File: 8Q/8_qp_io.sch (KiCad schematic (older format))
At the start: 0 parts

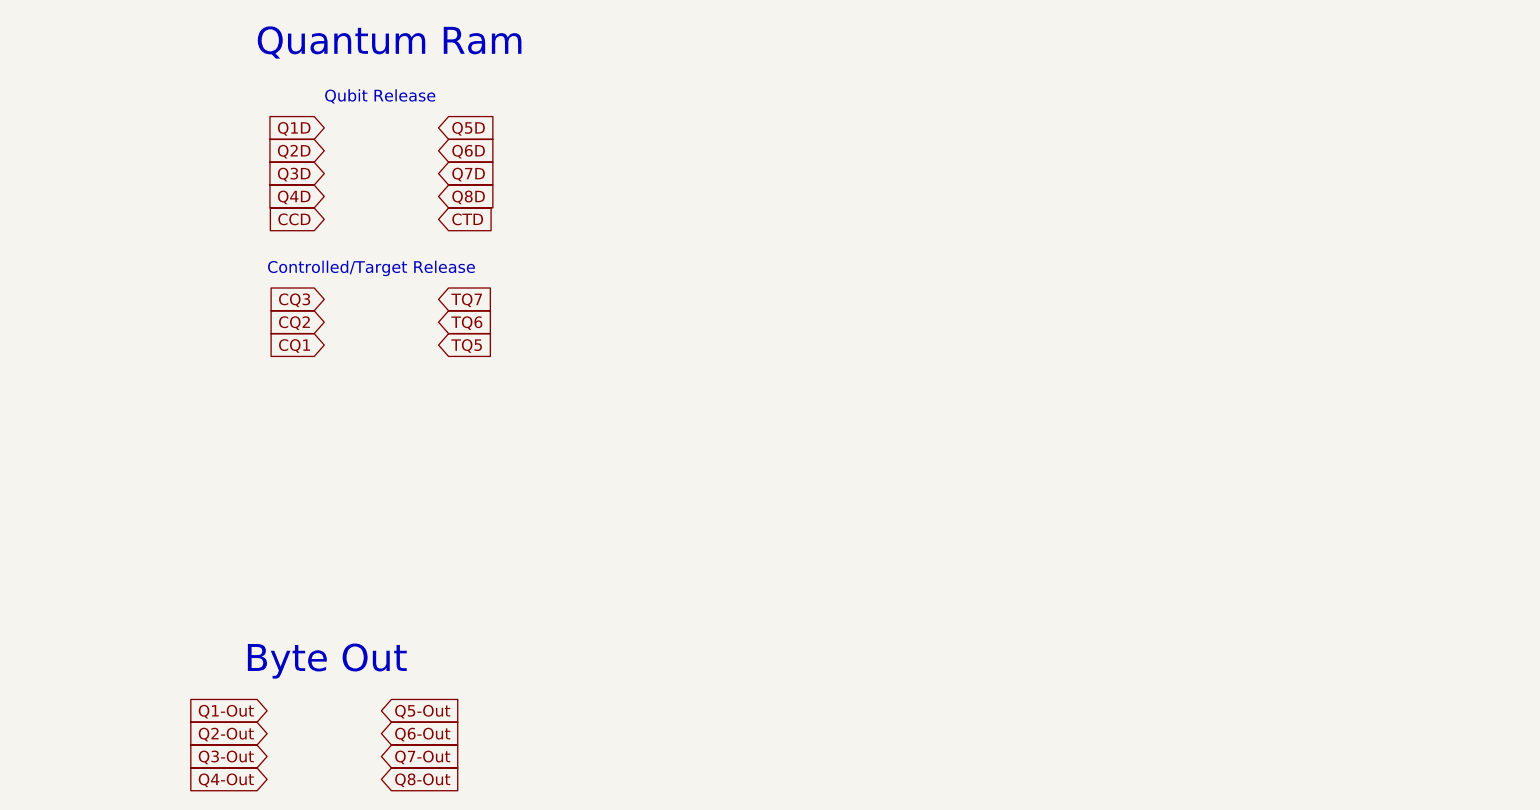
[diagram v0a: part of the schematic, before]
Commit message: modified:   8Q/8Q-cache.lib 	modified:   8Q/8Q.sch 	modified:   8Q/8_qp_io.sch 	new file:   8Q/RAM.sch 	deleted:    8Q/_saved_RAM.sch 	modified:   8Q/cpu.sch 	modified:   8Q/cpu_power.sch 	modified:   8Q/power.sch 	modified:   8Q/preprocessor.sch 	modified:   8Q/qpower.sch 	modified:   8Q/qpu.sch 	new file:   8q.dia 	modified:   README.md 	new file:   docs/source/imgs/8q.png
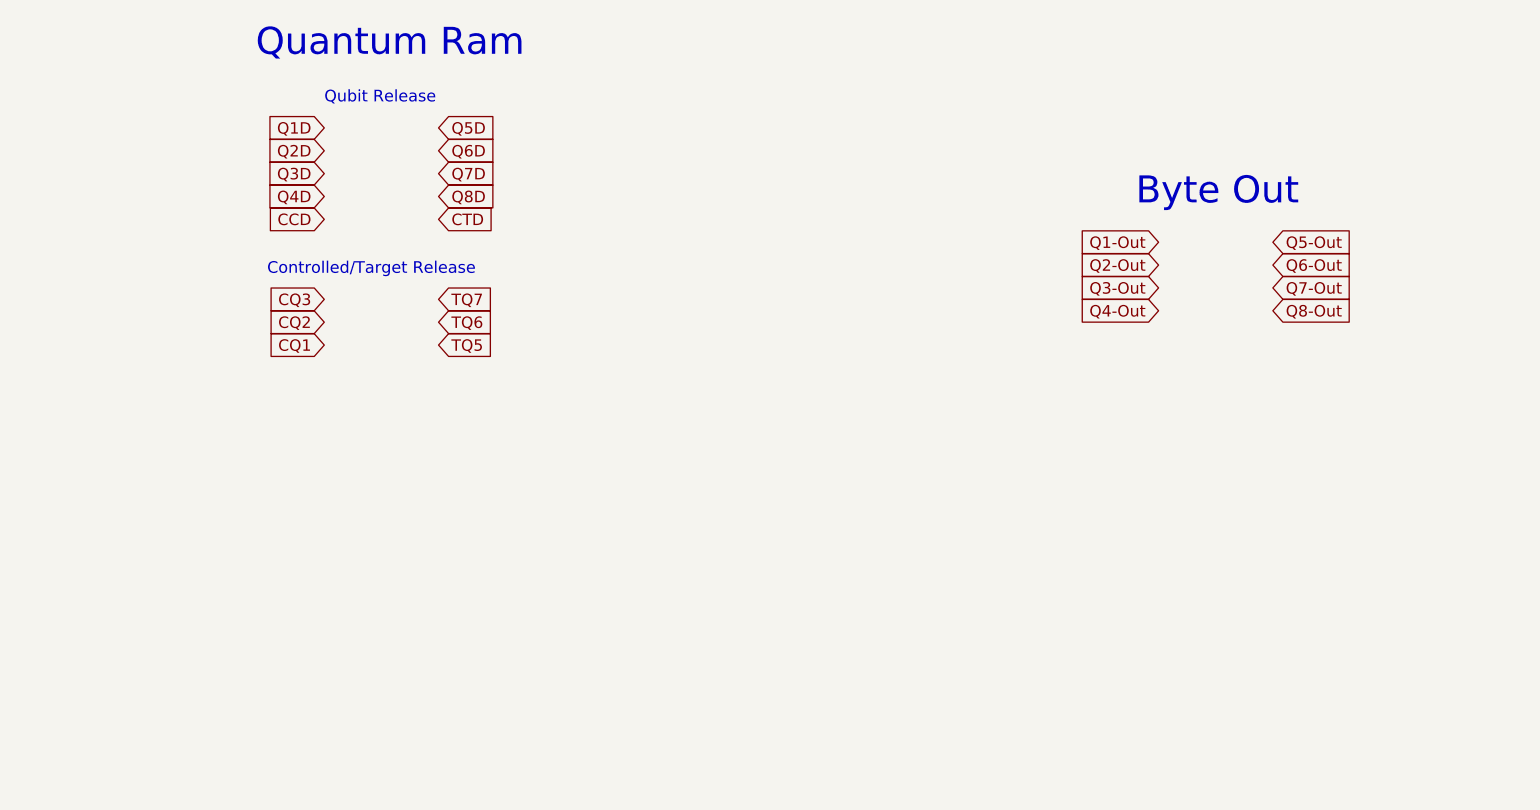
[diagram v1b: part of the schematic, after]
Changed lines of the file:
@@
 $Descr A4 11693 8268
 encoding utf-8
-Sheet 7 8
+Sheet 8 9
 Title ""
 Date ""
@@
 Text GLabel 9700 2450 0    50   Input ~ 0
 SWAP
-Text GLabel 5250 6200 0    50   Input ~ 0
+Text GLabel 9150 4150 0    50   Input ~ 0
 Q1-Out
 Text GLabel 1600 4600 0    50   Input ~ 0
 Q1-S
-Text GLabel 5250 6300 0    50   Input ~ 0
+Text GLabel 9150 4250 0    50   Input ~ 0
 Q2-Out
 Text GLabel 1600 4700 0    50   Input ~ 0
 Q2-S
-Text GLabel 5250 6400 0    50   Input ~ 0
+Text GLabel 9150 4350 0    50   Input ~ 0
 Q3-Out
 Text GLabel 1600 4800 0    50   Input ~ 0
 Q3-S
-Text GLabel 5250 6500 0    50   Input ~ 0
+Text GLabel 9150 4450 0    50   Input ~ 0
 Q4-Out
 Text GLabel 1600 4900 0    50   Input ~ 0
 Q4-S
-Text GLabel 5750 6200 2    50   Input ~ 0
+Text GLabel 9650 4150 2    50   Input ~ 0
 Q5-Out
 Text GLabel 2100 4600 2    50   Input ~ 0
 Q5-S
-Text GLabel 5750 6300 2    50   Input ~ 0
+Text GLabel 9650 4250 2    50   Input ~ 0
 Q6-Out
 Text GLabel 2100 4700 2    50   Input ~ 0
 Q6-S
-Text GLabel 5750 6400 2    50   Input ~ 0
+Text GLabel 9650 4350 2    50   Input ~ 0
 Q7-Out
 Text GLabel 2100 4800 2    50   Input ~ 0
 Q7-S
-Text GLabel 5750 6500 2    50   Input ~ 0
+Text GLabel 9650 4450 2    50   Input ~ 0
 Q8-Out
 Text GLabel 2100 4900 2    50   Input ~ 0
@@
 Text Notes 900  4450 0    118  ~ 0
 Post-Processing Data
-Text Notes 5150 6050 0    118  ~ 0
+Text Notes 9050 4000 0    118  ~ 0
 Byte Out
 Text Notes 1250 1700 0    118  ~ 0

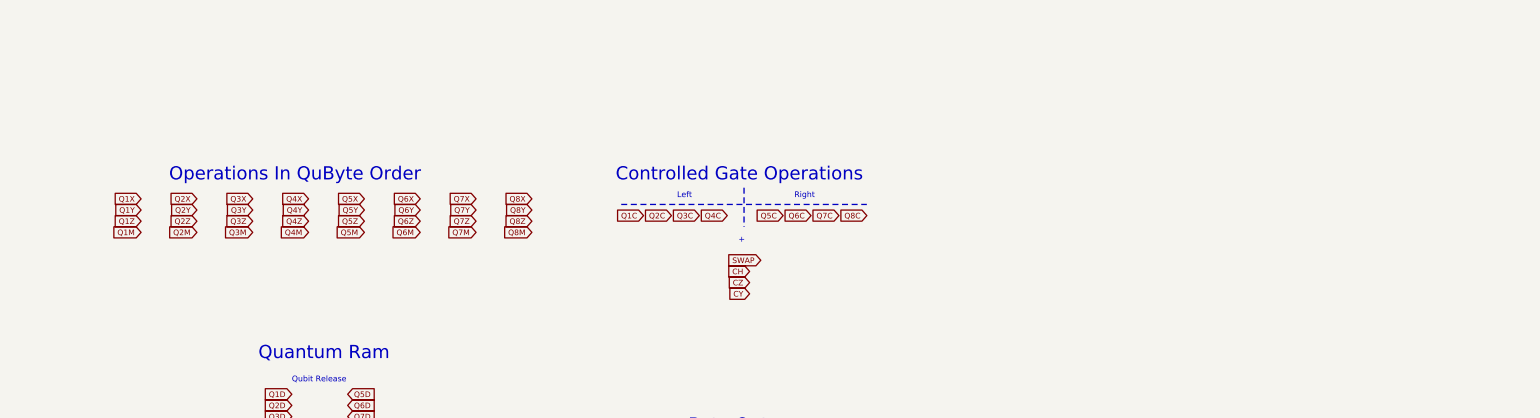
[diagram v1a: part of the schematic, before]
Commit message: modified:   8Q/8Q-cache.lib 	modified:   8Q/8Q.sch 	modified:   8Q/8_qp_io.sch 	modified:   8Q/RAM.sch 	new file:   8Q/control_logic.sch 	modified:   8Q/cpu.sch 	modified:   8Q/cpu_power.sch 	new file:   8Q/inorder.sch 	new file:   8Q/instruction_bus.sch 	new file:   8Q/output_cache.sch 	modified:   8Q/power.sch 	modified:   8Q/preprocessor.sch 	modified:   8Q/qpower.sch 	modified:   8Q/qpu.sch 	new file:   Controller.md 	modified:   QCore.md 	new file:   QPU_Operation.md 	new file:   docs/source/imgs/Screenshot from 2020-07-07 18-04-51.png 	new file:   tools/photon_birth_death.py 	new file:   tools/processor.py
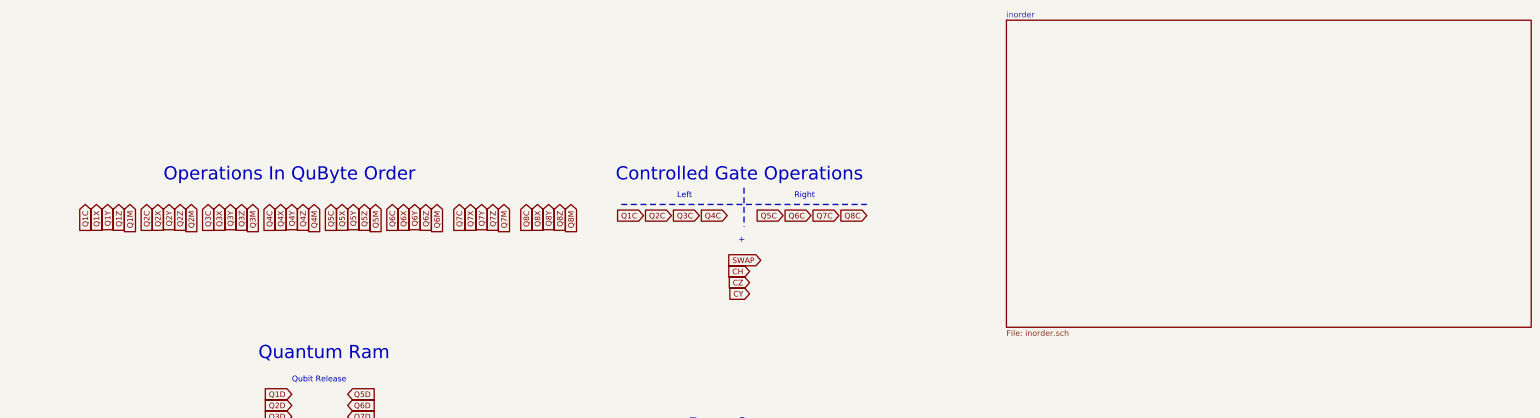
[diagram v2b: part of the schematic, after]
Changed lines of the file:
@@
 $Descr A4 11693 8268
 encoding utf-8
-Sheet 8 9
+Sheet 8 13
 Title ""
 Date ""
@@
 Comment4 ""
 $EndDescr
-Text GLabel 4150 1900 0    50   Input ~ 0
+Text GLabel 3750 1950 3    50   Input ~ 0
 Q1X
-Text GLabel 4150 2000 0    50   Input ~ 0
+Text GLabel 3850 1950 3    50   Input ~ 0
 Q1Y
-Text GLabel 4150 2100 0    50   Input ~ 0
+Text GLabel 3950 1950 3    50   Input ~ 0
 Q1Z
 Text GLabel 5500 3650 0    50   Input ~ 0
@@
 Text GLabel 5500 4050 0    50   Input ~ 0
 CCD
-Text GLabel 4650 1900 0    50   Input ~ 0
+Text GLabel 4300 1950 3    50   Input ~ 0
 Q2X
-Text GLabel 4650 2000 0    50   Input ~ 0
+Text GLabel 4400 1950 3    50   Input ~ 0
 Q2Y
-Text GLabel 4650 2100 0    50   Input ~ 0
+Text GLabel 4500 1950 3    50   Input ~ 0
 Q2Z
-Text GLabel 5150 1900 0    50   Input ~ 0
+Text GLabel 4850 1950 3    50   Input ~ 0
 Q3X
-Text GLabel 5150 2000 0    50   Input ~ 0
+Text GLabel 4950 1950 3    50   Input ~ 0
 Q3Y
-Text GLabel 5150 2100 0    50   Input ~ 0
+Text GLabel 5050 1950 3    50   Input ~ 0
 Q3Z
-Text GLabel 5650 1900 0    50   Input ~ 0
+Text GLabel 5400 1950 3    50   Input ~ 0
 Q4X
-Text GLabel 5650 2000 0    50   Input ~ 0
+Text GLabel 5500 1950 3    50   Input ~ 0
 Q4Y
-Text GLabel 5650 2100 0    50   Input ~ 0
+Text GLabel 5600 1950 3    50   Input ~ 0
 Q4Z
-Text GLabel 6150 1900 0    50   Input ~ 0
+Text GLabel 5950 1950 3    50   Input ~ 0
 Q5X
-Text GLabel 6150 2000 0    50   Input ~ 0
+Text GLabel 6050 1950 3    50   Input ~ 0
 Q5Y
-Text GLabel 6150 2100 0    50   Input ~ 0
+Text GLabel 6150 1950 3    50   Input ~ 0
 Q5Z
-Text GLabel 6650 1900 0    50   Input ~ 0
+Text GLabel 6500 1950 3    50   Input ~ 0
 Q6X
-Text GLabel 6650 2000 0    50   Input ~ 0
+Text GLabel 6600 1950 3    50   Input ~ 0
 Q6Y
-Text GLabel 6650 2100 0    50   Input ~ 0
+Text GLabel 6700 1950 3    50   Input ~ 0
 Q6Z
-Text GLabel 7150 1900 0    50   Input ~ 0
+Text GLabel 7100 1950 3    50   Input ~ 0
 Q7X
-Text GLabel 7150 2000 0    50   Input ~ 0
+Text GLabel 7200 1950 3    50   Input ~ 0
 Q7Y
-Text GLabel 7150 2100 0    50   Input ~ 0
+Text GLabel 7300 1950 3    50   Input ~ 0
 Q7Z
-Text GLabel 7650 1900 0    50   Input ~ 0
+Text GLabel 7700 1950 3    50   Input ~ 0
 Q8X
-Text GLabel 7650 2000 0    50   Input ~ 0
+Text GLabel 7800 1950 3    50   Input ~ 0
 Q8Y
-Text GLabel 7650 2100 0    50   Input ~ 0
+Text GLabel 7900 1950 3    50   Input ~ 0
 Q8Z
 Text GLabel 6000 4050 2    50   Input ~ 0
@@
 Text GLabel 6000 3650 2    50   Input ~ 0
 Q5D
-Text GLabel 4150 2200 0    50   Input ~ 0
+Text GLabel 4050 1950 3    50   Input ~ 0
 Q1M
-Text GLabel 4650 2200 0    50   Input ~ 0
+Text GLabel 4600 1950 3    50   Input ~ 0
 Q2M
-Text GLabel 5150 2200 0    50   Input ~ 0
+Text GLabel 5150 1950 3    50   Input ~ 0
 Q3M
-Text GLabel 5650 2200 0    50   Input ~ 0
+Text GLabel 5700 1950 3    50   Input ~ 0
 Q4M
-Text GLabel 6150 2200 0    50   Input ~ 0
+Text GLabel 6250 1950 3    50   Input ~ 0
 Q5M
-Text GLabel 6650 2200 0    50   Input ~ 0
+Text GLabel 6800 1950 3    50   Input ~ 0
 Q6M
-Text GLabel 7150 2200 0    50   Input ~ 0
+Text GLabel 7400 1950 3    50   Input ~ 0
 Q7M
-Text GLabel 7650 2200 0    50   Input ~ 0
+Text GLabel 8000 1950 3    50   Input ~ 0
 Q8M
 Text GLabel 9600 2750 0    50   Input ~ 0
@@
 Text GLabel 10650 2050 0    50   Input ~ 0
 Q8C
-Text Notes 4400 1750 0    118  ~ 0
+Text Notes 4350 1750 0    118  ~ 0
 Operations In QuByte Order
 Text Notes 900  4450 0    118  ~ 0
@@
 Text Notes 10000 1900 0    51   ~ 0
 Right
+Text GLabel 3650 1950 3    50   Input ~ 0
+Q1C
+Text GLabel 4200 1950 3    50   Input ~ 0
+Q2C
+Text GLabel 5300 1950 3    50   Input ~ 0
+Q4C
+Text GLabel 4750 1950 3    50   Input ~ 0
+Q3C
+Text GLabel 5850 1950 3    50   Input ~ 0
+Q5C
+Text GLabel 6400 1950 3    50   Input ~ 0
+Q6C
+Text GLabel 7000 1950 3    50   Input ~ 0
+Q7C
+Text GLabel 7600 1950 3    50   Input ~ 0
+Q8C
+$Sheet
+S 11900 300  4700 2750
+U 5F935B1A
+F0 "inorder" 51
+F1 "inorder.sch" 51
+$EndSheet
 $EndSCHEMATC
